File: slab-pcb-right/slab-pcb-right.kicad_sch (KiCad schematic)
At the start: 87 parts, among them J1 Conn_01x04, J2 Conn_01x04, J3 TRRS_L, J4 TRRS_R, J5 SSD1306, SW1 RotaryEncoder, U1 Seeeduino Xiao rp2040, U2 PCA9555PW, U3 PCA9555PW, U4 ADS1110, U5 SN74AHCT125PWR, U6 TCA4307DGKR

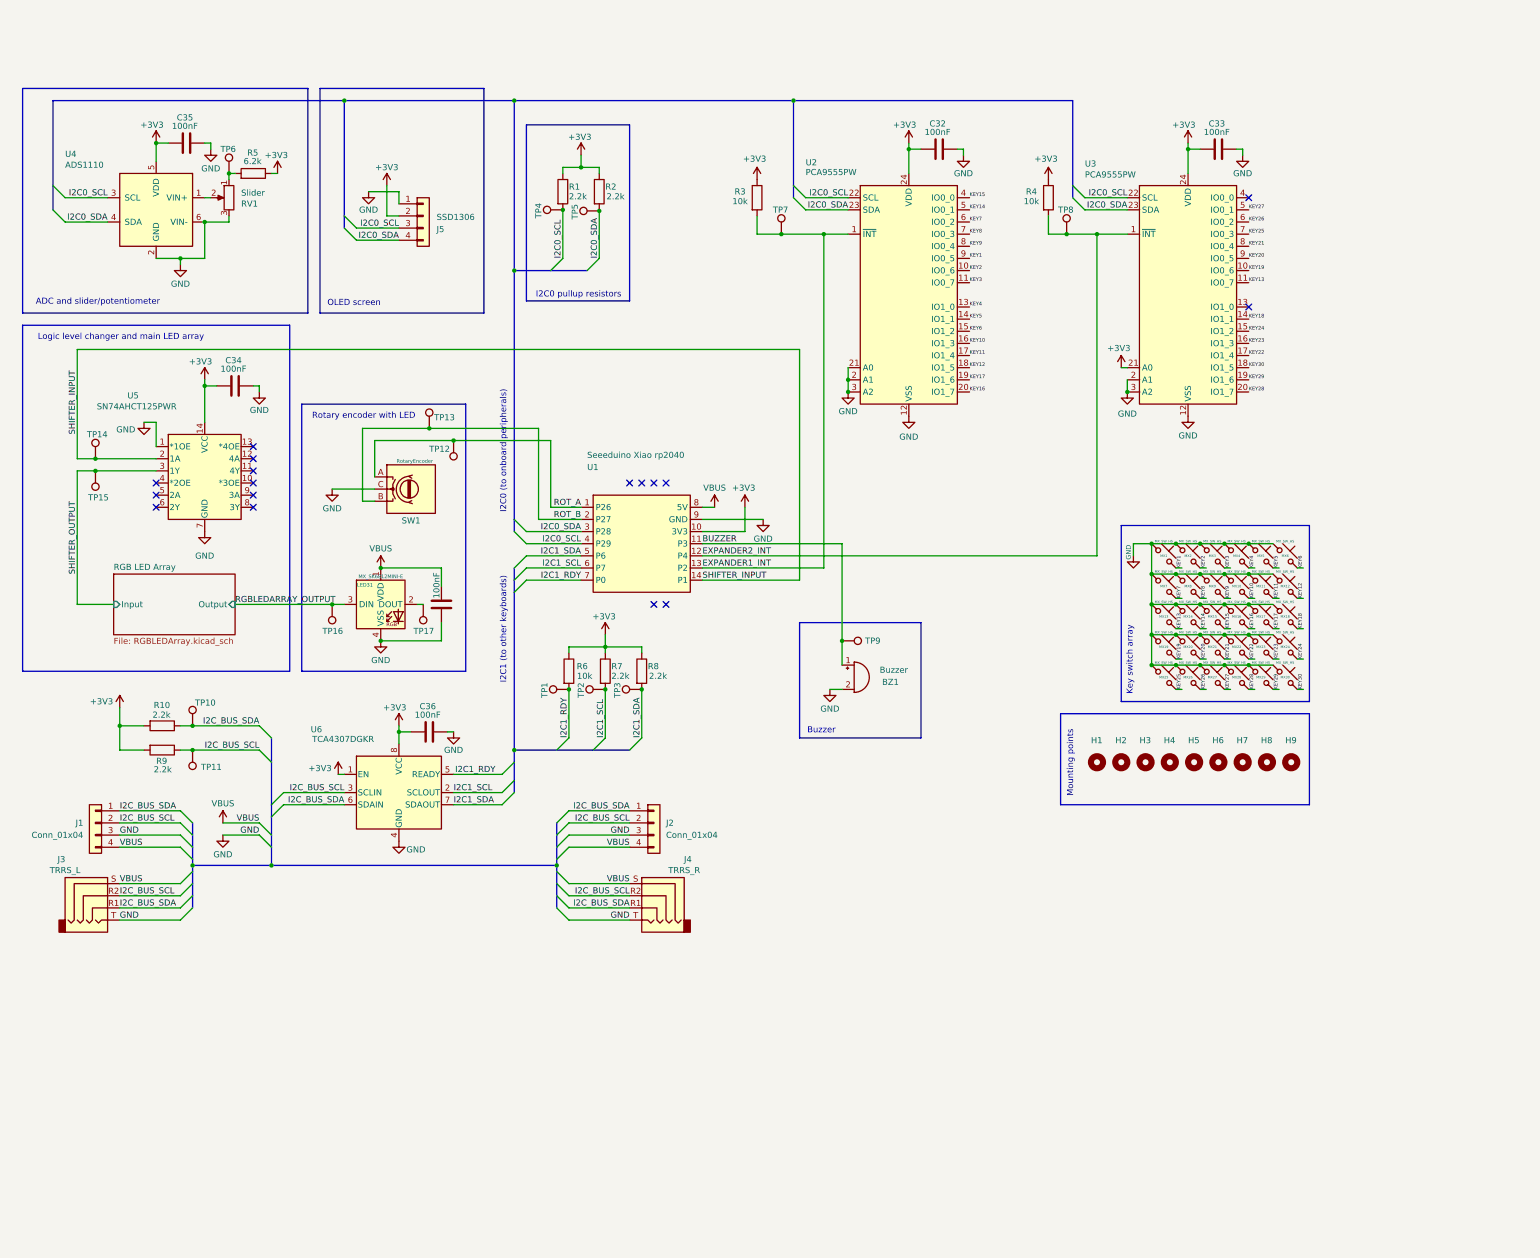
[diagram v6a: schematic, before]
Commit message: feat: restart slab-pcb-right routing, allign components
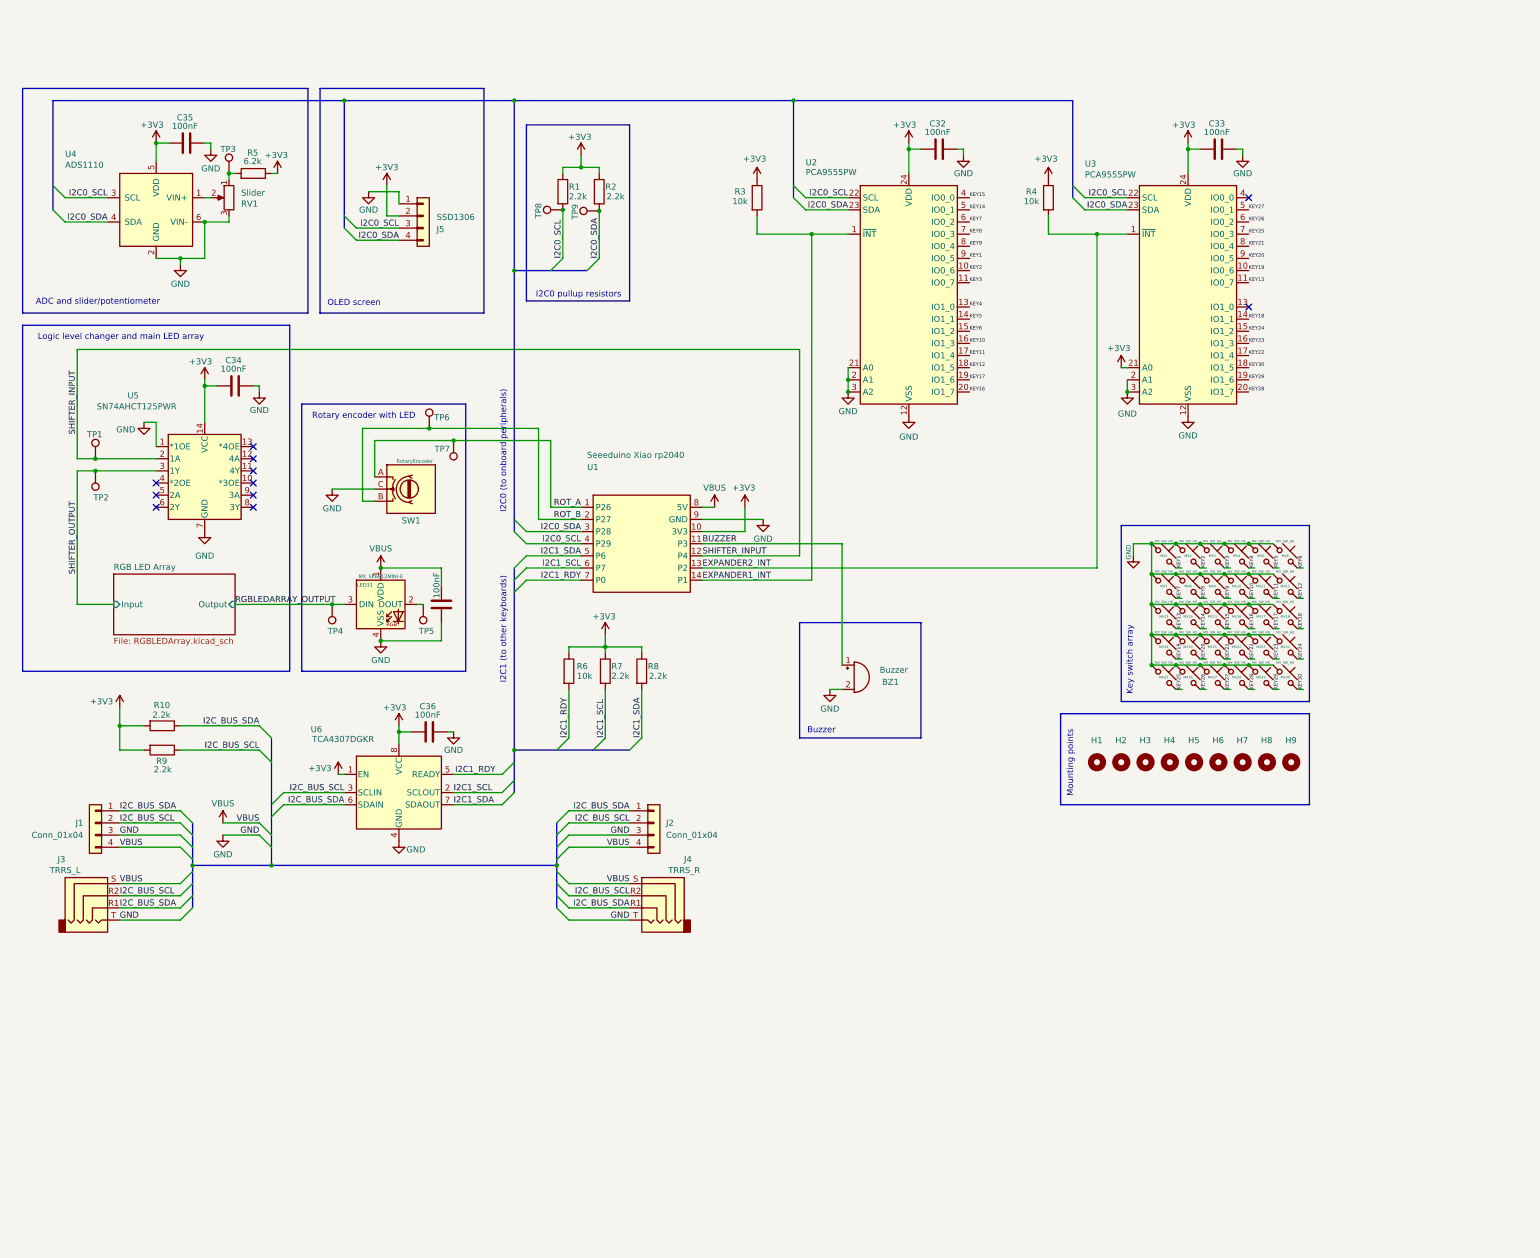
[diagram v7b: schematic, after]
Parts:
- removed TP1, TP10, TP11, TP2, TP3, TP7, TP8, TP9: TestPoint, TestPoint:TestPoint_Pad_D1.5mm, symbol Connector:TestPoint
- renumbered TP14 to TP1, TP15 to TP2, TP6 to TP3, TP16 to TP4, TP17 to TP5, TP13 to TP6, TP12 to TP7, TP4 to TP8, TP5 to TP9
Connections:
- net EXPANDER1_INT: now also U1.14 (P1); no longer U1.13 (P2)
- net EXPANDER2_INT: now also U1.13 (P2); no longer U1.12 (P4)
- net SHIFTER_INPUT: now also U1.12 (P4); no longer U1.14 (P1)
- no-connect marks 17 -> 11
